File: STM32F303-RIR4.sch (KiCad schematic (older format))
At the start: 10 parts, among them J0 CN7, J1 CN10, J101 LCC, J102 LCC, U101 SN65HVD1050

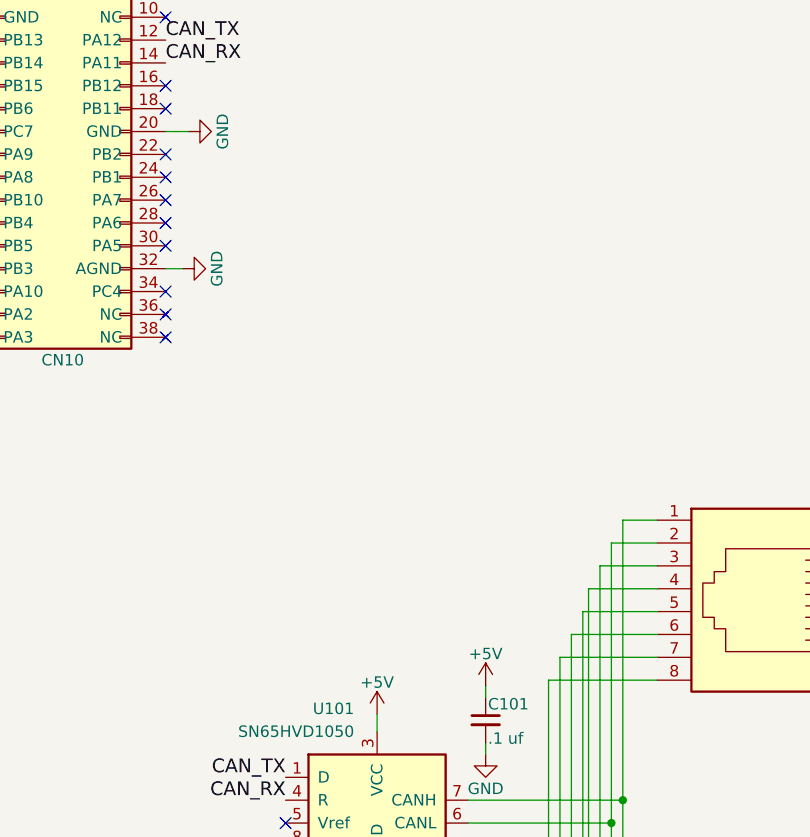
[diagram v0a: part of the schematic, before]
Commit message: Add activity LEDS.
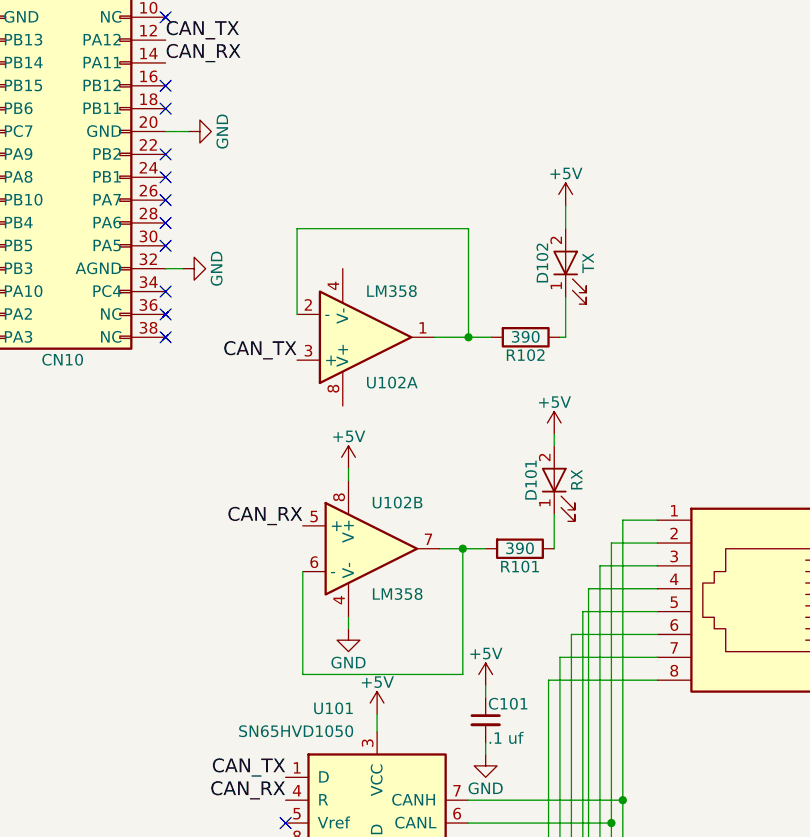
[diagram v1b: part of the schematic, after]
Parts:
- added D101: RX, LEDs:LED_0603, symbol LED
- added D102: TX, LEDs:LED_0603, symbol LED
- added R101, R102: 390, Resistors_SMD:R_0603, symbol R
- added U102: LM358, Housings_SOIC:SOIC-8_3.9x4.9mm_Pitch1.27mm, symbol LM358
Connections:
- net +5V: now also D101.2 (A), D102.2 (A), U102.8 (V+)
- net CAN_RX: now also U102.5 (+)
- net CAN_TX: now also U102.3 (+)
- net GND: now also U102.4 (V-)
- new net: R102.2, U102.1, U102.2 (-)
- new net: R101.2, U102.6 (-), U102.7
- new net: D102.1 (K), R102.1
- new net: D101.1 (K), R101.1
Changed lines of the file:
@@
 	1    0    0    -1
 $EndComp
+$Comp
+L LM358 U102
+U 1 1 642C3F7A
+P 7600 3100
+F 0 "U102" H 7600 3300 50  0000 L CNN
+F 1 "LM358" H 7600 2900 50  0000 L CNN
+F 2 "Housings_SOIC:SOIC-8_3.9x4.9mm_Pitch1.27mm" H 7600 3100 50  0001 C CNN
+F 3 "" H 7600 3100 50  0001 C CNN
+F 4 "595-LM358DR" H 7600 3100 60  0001 C CNN "Mouser Part Number"
+	1    7600 3100
+	1    0    0    1
+$EndComp
+$Comp
+L LM358 U102
+U 2 1 642C4128
+P 7625 4025
+F 0 "U102" H 7625 4225 50  0000 L CNN
+F 1 "LM358" H 7625 3825 50  0000 L CNN
+F 2 "Housings_SOIC:SOIC-8_3.9x4.9mm_Pitch1.27mm" H 7625 4025 50  0001 C CNN
+F 3 "" H 7625 4025 50  0001 C CNN
+F 4 "595-LM358DR" H 7625 4025 60  0001 C CNN "Mouser Part Number"
+	2    7625 4025
+	1    0    0    -1
+$EndComp
+Wire Wire Line
+	7300 3000 7300 2625
+Wire Wire Line
+	7300 2625 8050 2625
+Wire Wire Line
+	8050 2625 8050 3100
+Wire Wire Line
+	7900 3100 8150 3100
+Wire Wire Line
+	7325 4125 7325 4575
+Wire Wire Line
+	7325 4575 8025 4575
+Wire Wire Line
+	8025 4575 8025 4025
+Wire Wire Line
+	7925 4025 8125 4025
+Text Label 7325 3925 2    60   ~ 0
+CAN_RX
+Text Label 7300 3200 2    60   ~ 0
+CAN_TX
+$Comp
+L +5V #PWR015
+U 1 1 642C4BAF
+P 7525 3675
+F 0 "#PWR015" H 7525 3525 50  0001 C CNN
+F 1 "+5V" H 7525 3815 50  0000 C CNN
+F 2 "" H 7525 3675 50  0001 C CNN
+F 3 "" H 7525 3675 50  0001 C CNN
+	1    7525 3675
+	1    0    0    -1
+$EndComp
+Wire Wire Line
+	7525 3675 7525 3725
+$Comp
+L GND #PWR016
+U 1 1 642C4C57
+P 7525 4375
+F 0 "#PWR016" H 7525 4125 50  0001 C CNN
+F 1 "GND" H 7525 4225 50  0000 C CNN
+F 2 "" H 7525 4375 50  0001 C CNN
+F 3 "" H 7525 4375 50  0001 C CNN
+	1    7525 4375
+	1    0    0    -1
+$EndComp
+Wire Wire Line
+	7525 4325 7525 4375
+$Comp
+L R R102
+U 1 1 642C522C
+P 8300 3100
+F 0 "R102" V 8380 3100 50  0000 C CNN
+F 1 "390" V 8300 3100 50  0000 C CNN
+F 2 "Resistors_SMD:R_0603" V 8230 3100 50  0001 C CNN
+F 3 "" H 8300 3100 50  0001 C CNN
+F 4 "603-AC0603JR-07390RL" V 8300 3100 60  0001 C CNN "Mouser Part Number"
+	1    8300 3100
+	0    1    1    0
+$EndComp
+$Comp
+L R R101
+U 1 1 642C53B6
+P 8275 4025
+F 0 "R101" V 8355 4025 50  0000 C CNN
+F 1 "390" V 8275 4025 50  0000 C CNN
+F 2 "Resistors_SMD:R_0603" V 8205 4025 50  0001 C CNN
+F 3 "" H 8275 4025 50  0001 C CNN
+F 4 "603-AC0603JR-07390RL" V 8275 4025 60  0001 C CNN "Mouser Part Number"
+	1    8275 4025
+	0    1    1    0
+$EndComp
+Connection ~ 8050 3100
+Connection ~ 8025 4025
+$Comp
+L LED D101
+U 1 1 642C5EE3
+P 8425 3725
+F 0 "D101" H 8425 3825 50  0000 C CNN
+F 1 "RX" H 8425 3625 50  0000 C CNN
+F 2 "LEDs:LED_0603" H 8425 3725 50  0001 C CNN
+F 3 "" H 8425 3725 50  0001 C CNN
+F 4 "710-150060YS75000" H 8425 3725 60  0001 C CNN "Mouser Part Number"
+	1    8425 3725
+	0    -1   -1   0
+$EndComp
+Wire Wire Line
+	8425 3875 8425 4025
+$Comp
+L +5V #PWR017
+U 1 1 642C62DD
+P 8425 3525
+F 0 "#PWR017" H 8425 3375 50  0001 C CNN
+F 1 "+5V" H 8425 3665 50  0000 C CNN
+F 2 "" H 8425 3525 50  0001 C CNN
+F 3 "" H 8425 3525 50  0001 C CNN
+	1    8425 3525
+	1    0    0    -1
+$EndComp
+Wire Wire Line
+	8425 3525 8425 3575
+$Comp
+L LED D102
+U 1 1 642C64EA
+P 8475 2775
+F 0 "D102" H 8475 2875 50  0000 C CNN
+F 1 "TX" H 8475 2675 50  0000 C CNN
+F 2 "LEDs:LED_0603" H 8475 2775 50  0001 C CNN
+F 3 "" H 8475 2775 50  0001 C CNN
+F 4 "710-150060SS75000" H 8475 2775 60  0001 C CNN "Mouser Part Number"
+	1    8475 2775
+	0    -1   -1   0
+$EndComp
+$Comp
+L +5V #PWR018
+U 1 1 642C6635
+P 8475 2525
+F 0 "#PWR018" H 8475 2375 50  0001 C CNN
+F 1 "+5V" H 8475 2665 50  0000 C CNN
+F 2 "" H 8475 2525 50  0001 C CNN
+F 3 "" H 8475 2525 50  0001 C CNN
+	1    8475 2525
+	1    0    0    -1
+$EndComp
+Wire Wire Line
+	8475 2925 8475 3100
+Wire Wire Line
+	8475 3100 8450 3100
+Wire Wire Line
+	8475 2525 8475 2625
 $EndSCHEMATC

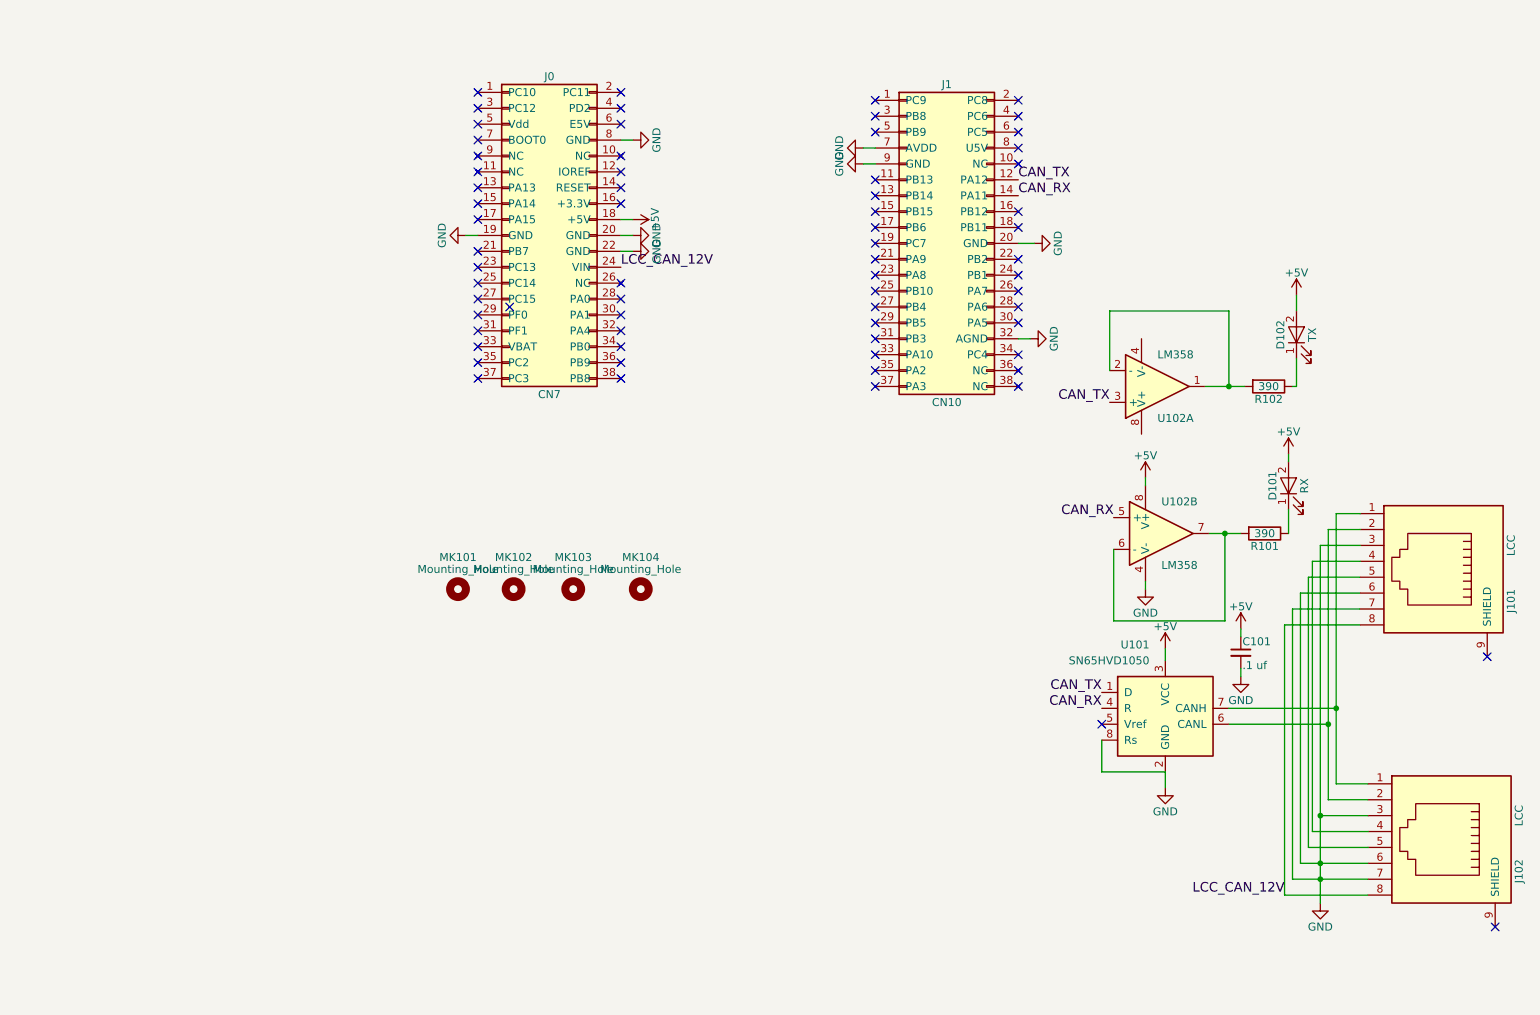
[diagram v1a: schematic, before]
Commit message: Add additional outputs (crossing controls).
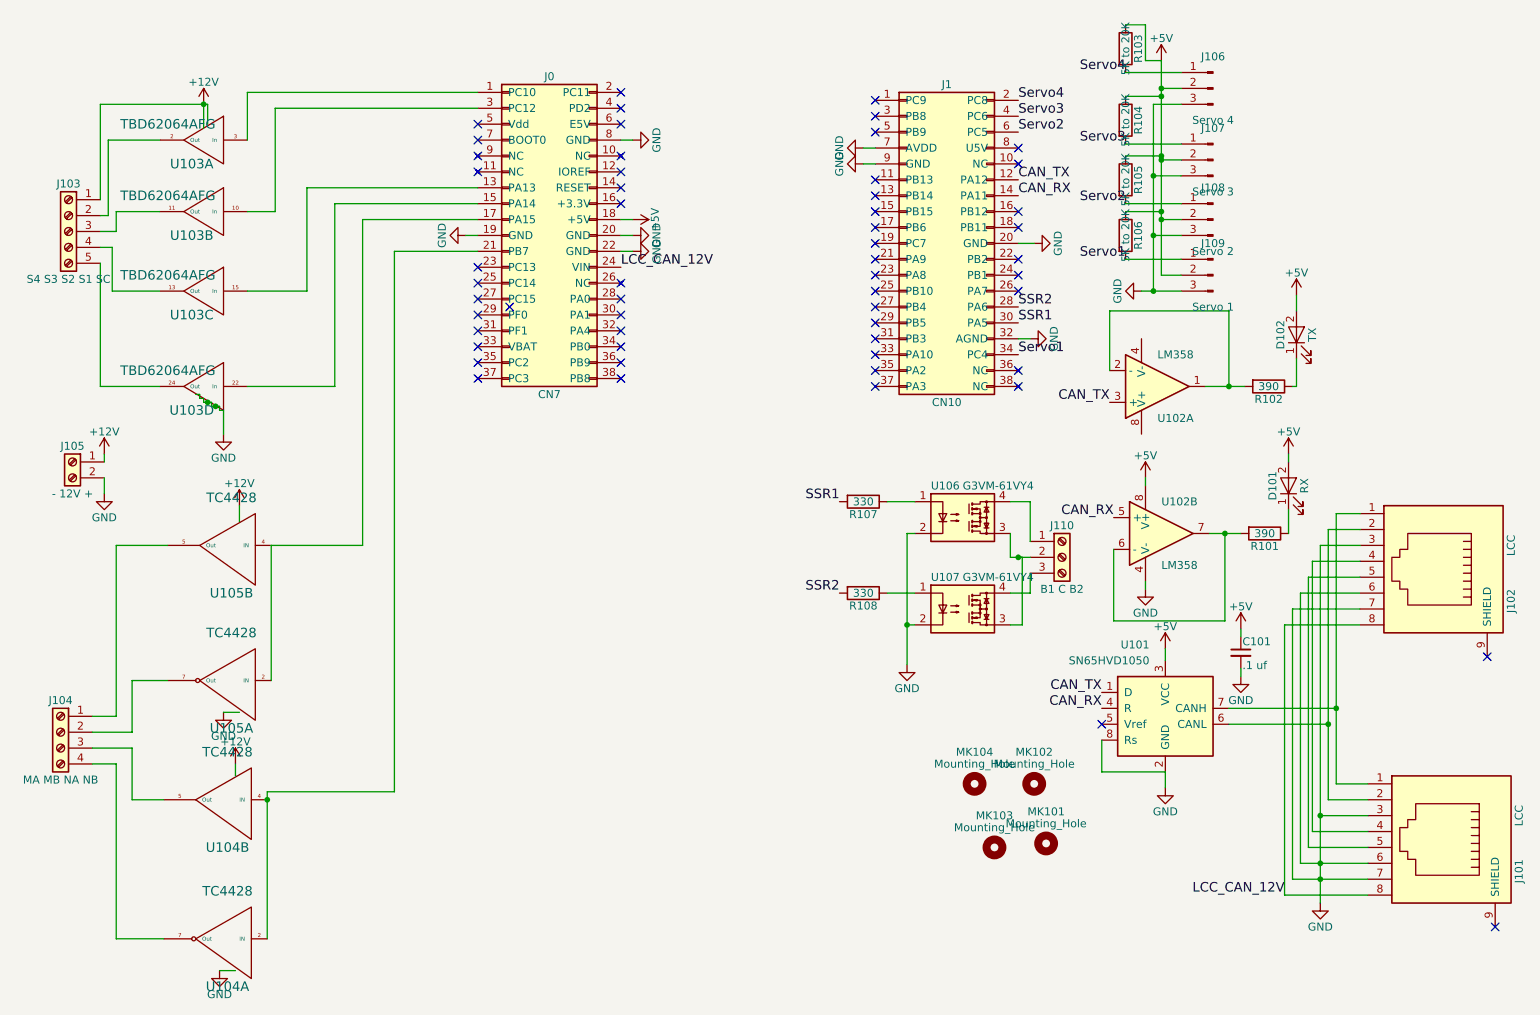
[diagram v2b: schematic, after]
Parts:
- added J103: S4 S3 S2 S1 SC, Terminal_Blocks:TerminalBlock_Pheonix_MPT-2.54mm_5pol, symbol Screw_Terminal_01x05
- added J104: MA MB NA NB, Terminal_Blocks:TerminalBlock_Pheonix_MPT-2.54mm_4pol, symbol Screw_Terminal_01x04
- added J105: - 12V +, Terminal_Blocks:TerminalBlock_Pheonix_PT-3.5mm_2pol, symbol Screw_Terminal_01x02
- added J106: Servo 4, Pin_Headers:Pin_Header_Straight_1x03_Pitch2.54mm, symbol Conn_01x03_Male
- added J107: Servo 3, Pin_Headers:Pin_Header_Straight_1x03_Pitch2.54mm, symbol Conn_01x03_Male
- added J108: Servo 2, Pin_Headers:Pin_Header_Straight_1x03_Pitch2.54mm, symbol Conn_01x03_Male
- added J109: Servo 1, Pin_Headers:Pin_Header_Straight_1x03_Pitch2.54mm, symbol Conn_01x03_Male
- added J110: B1 C B2, Terminal_Blocks:TerminalBlock_Pheonix_MPT-2.54mm_3pol, symbol Screw_Terminal_01x03
- added R103, R104, R105, R106: 5K to 20K, Resistors_THT:R_Axial_DIN0204_L3.6mm_D1.6mm_P7.62mm_Horizontal, symbol R
- added R107, R108: 330, Resistors_SMD:R_0603, symbol R
- added U103: TBD62064AFG, SOP100P800X190:SOP100P800X190-24N, symbol TBD62064AFG
- added U104, U105: TC4428, Housings_SOIC:SOIC-8_3.9x4.9mm_Pitch1.27mm, symbol TC4428
- added U106, U107: G3VM-61VY4, Housings_SOIC:SO-4_4.4x4.3mm_Pitch2.54mm, symbol ASSR-1218
- renumbered J102 to J101, J101 to J102
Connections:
- net +5V: now also J106.2 (Pin_2), J107.2 (Pin_2), J108.2 (Pin_2), J109.2 (Pin_2), R103.1, R104.1, R105.1, R106.1
- net GND: now also J105.2 (Pin_2), J106.3 (Pin_3), J107.3 (Pin_3), J108.3 (Pin_3), J109.3 (Pin_3), U103.17 (GND), U103.18 (GND), U103.19 (GND), U103.20 (GND), U103.5 (GND), U103.6 (GND), U103.7 (GND), U103.8 (GND), U104.3 (GND), U104.3 (GND), U105.3 (GND), U105.3 (GND), U106.2, U107.2
- net at J0.1 (PC10): now also U103.3 (In)
- net at J0.13 (PA13): now also U103.15 (In)
- net at J0.15 (PA14): now also U103.22 (In)
- net at J0.17 (PA15): now also U105.2 (IN), U105.4 (IN)
- net at J0.21 (PB7): now also U104.2 (IN), U104.4 (IN)
- net at J0.3 (PC12): now also U103.10 (In)
- net Servo4: now reaches J1.2 (PC8)
- net Servo4: now also J106.1 (Pin_1), R103.2
- net SSR2: now reaches J1.28 (PA6)
- net SSR2: now also R108.2
- net SSR1: now reaches J1.30 (PA5)
- net SSR1: now also R107.2
- net Servo1: now reaches J1.34 (PC4)
- net Servo1: now also J109.1 (Pin_1), R106.2
- net Servo3: now reaches J1.4 (PC6)
- net Servo3: now also J107.1 (Pin_1), R104.2
- net Servo2: now reaches J1.6 (PC5)
- net Servo2: now also J108.1 (Pin_1), R105.2
- new net: J103.2 (Pin_2), U103.2 (Out)
- new net: J103.3 (Pin_3), U103.11 (Out)
- new net: J103.4 (Pin_4), U103.13 (Out)
- new net: J103.5 (Pin_5), U103.24 (Out)
- new net: J104.1 (Pin_1), U105.5 (Out)
- new net: J104.2 (Pin_2), U105.7 (Out)
- new net: J104.3 (Pin_3), U104.5 (Out)
- new net: J104.4 (Pin_4), U104.7 (Out)
- new net: R107.1, U106.1
- new net: J110.2 (Pin_2), U106.3, U107.3
- new net: J110.1 (Pin_1), U106.4
- new net: R108.1, U107.1
- new net: J110.3 (Pin_3), U107.4
- new net +12V: J103.1 (Pin_1), J105.1 (Pin_1), U103.1 (OC), U103.1 (OC), U103.1 (OC), U103.1 (OC), U103.12 (OC), U104.6 (Vdd), U104.6 (Vdd), U105.6 (Vdd), U105.6 (Vdd)
- no-connect marks 68 -> 56
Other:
- moved on the sheet: MK101, MK102, MK103, MK104
